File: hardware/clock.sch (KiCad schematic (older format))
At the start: 18 parts, among them P4 CLOCK_PANEL, P5 CLOCK_MAIN, U1 LM555N, U5 TL071, U6 LM2903

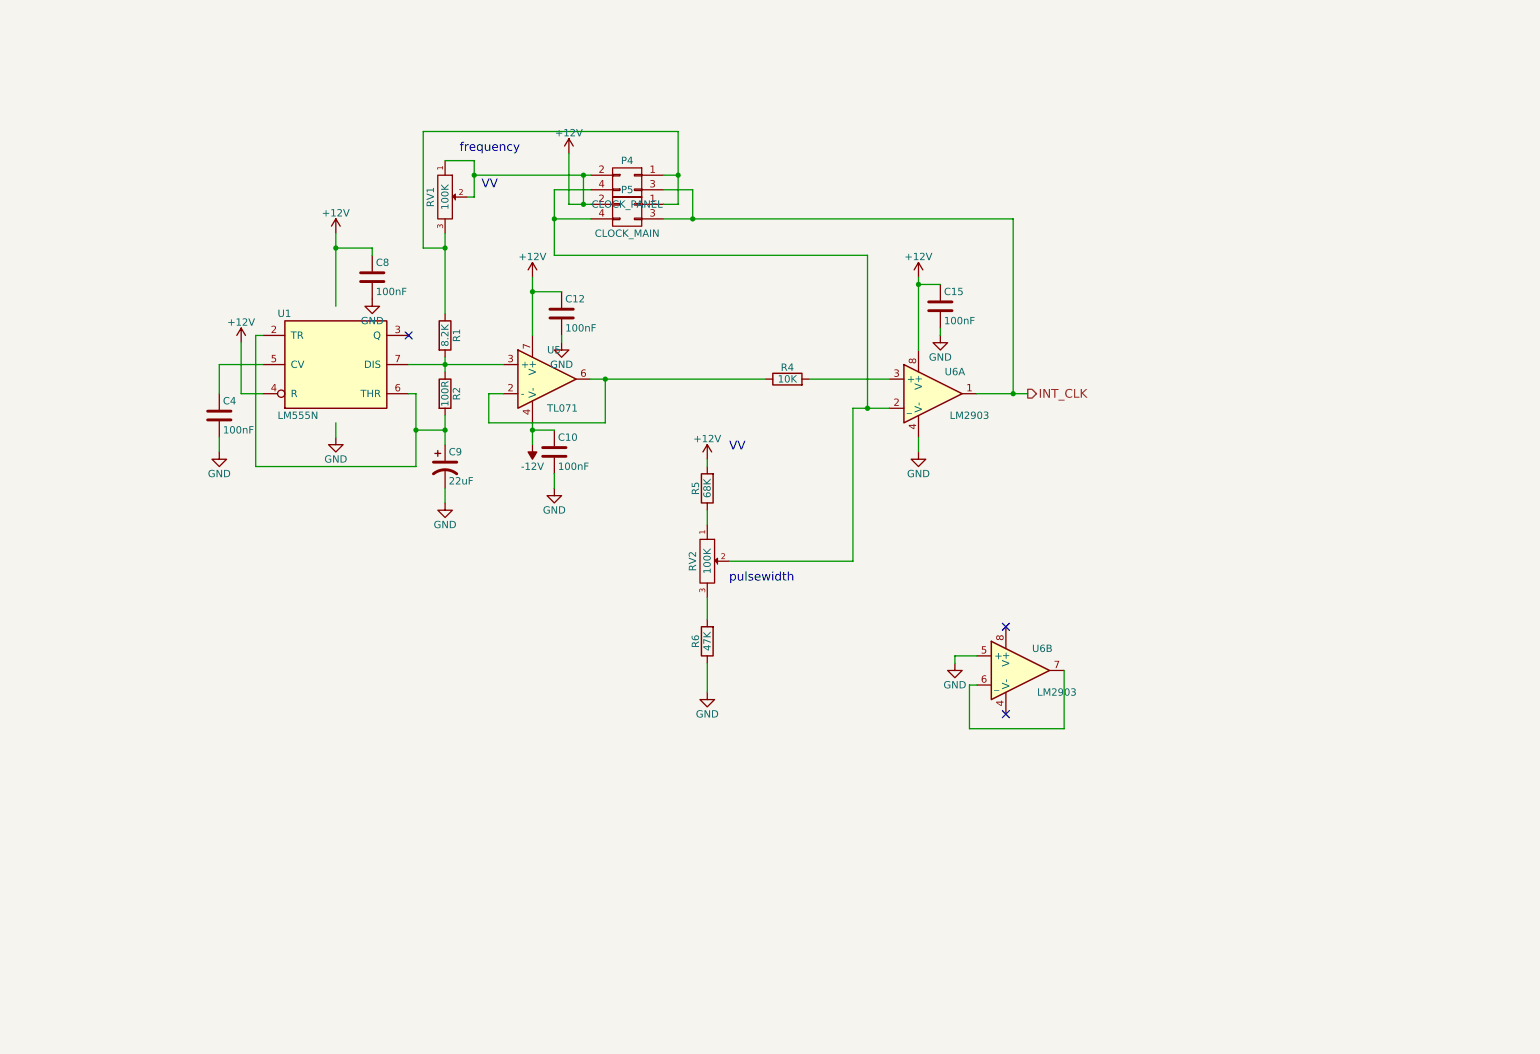
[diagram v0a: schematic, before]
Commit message: replaced old hardware files with the most recent ones tracking CLAUDE.md AI files used in revising the project
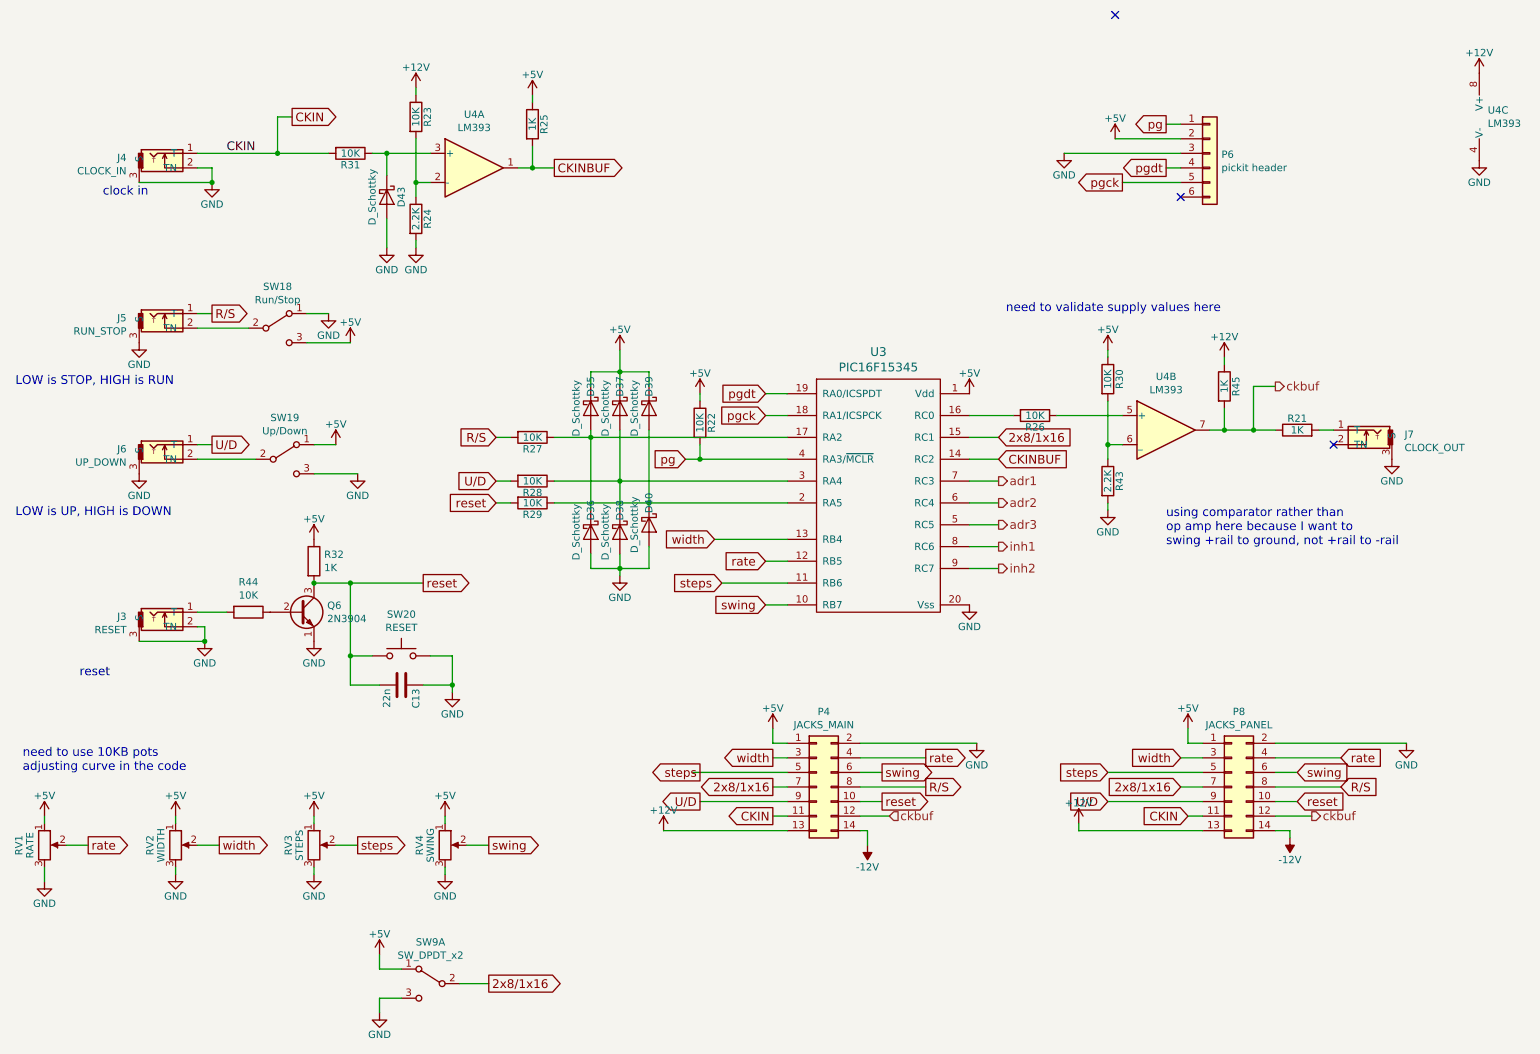
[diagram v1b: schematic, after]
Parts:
- removed C10, C12, C15, C4, C8: 100nF, Capacitors_ThroughHole:C_Rect_L7_W2_P5, symbol C
- removed C9: 22uF, Capacitors_ThroughHole:C_Radial_D5_L11_P2.5, symbol CP1
- removed P4: CLOCK_PANEL, Socket_Strips:Socket_Strip_Straight_2x02, symbol CONN_02X02
- removed P5: CLOCK_MAIN, Pin_Headers:Pin_Header_Straight_2x02, symbol CONN_02X02
- removed R1: 8.2K, Resistors_ThroughHole:Resistor_Horizontal_RM10mm, symbol R
- removed R2: 100R, Resistors_ThroughHole:Resistor_Horizontal_RM10mm, symbol R
- removed R4: 10K, Resistors_ThroughHole:Resistor_Horizontal_RM10mm, symbol R
- removed R5: 68K, Resistors_ThroughHole:Resistor_Horizontal_RM10mm, symbol R
- removed R6: 47K, Resistors_ThroughHole:Resistor_Horizontal_RM10mm, symbol R
- removed RV1, RV2: 100K, Walter Resistors:trimmer_alps-rk09k1130ah1, symbol POT-RESCUE-trigger-seq
- removed U1: LM555N, Housings_DIP:DIP-8_W7.62mm_LongPads, symbol LM555N
- removed U5: TL071, Housings_DIP:DIP-8_W7.62mm_LongPads, symbol TL071
- removed U6: LM2903, symbol LM2903
- added C13: 22n, Capacitor_THT:C_Disc_D7.0mm_W2.5mm_P5.00mm, symbol device:C
- added D35, D36, D37, D38, D39, D40, D43: D_Schottky, Diode_THT:D_DO-35_SOD27_P7.62mm_Horizontal, symbol device:D_Schottky
- added J3: RESET, My Library:thonkiconn, symbol altconnector:AudioJack2_Ground_Switch
- added J4: CLOCK_IN, My Library:thonkiconn, symbol altconnector:AudioJack2_Ground_Switch
- added J5: RUN_STOP, My Library:thonkiconn, symbol altconnector:AudioJack2_Ground_Switch
- added J6: UP_DOWN, My Library:thonkiconn, symbol altconnector:AudioJack2_Ground_Switch
- added J7: CLOCK_OUT, My Library:thonkiconn, symbol altconnector:AudioJack2_Ground_Switch
- added P4: JACKS_MAIN, Connector_PinHeader_2.54mm:PinHeader_2x07_P2.54mm_Vertical, symbol trigger-seq-rescue:Conn_02x07_Odd_Even-Connector
- added P6: pickit header, Connector_PinHeader_2.54mm:PinHeader_1x06_P2.54mm_Vertical, symbol trigger-seq-rescue:Conn_01x06-Connector
- added P8: JACKS_PANEL, Connector_PinSocket_2.54mm:PinSocket_2x07_P2.54mm_Vertical, symbol trigger-seq-rescue:Conn_02x07_Odd_Even-Connector
- added Q6: 2N3904, Package_TO_SOT_THT:TO-92_Inline_Wide, symbol trigger-seq-rescue:2N3904-Transistor
- added R21, R25, R32, R45: 1K, Resistor_THT:R_Axial_DIN0207_L6.3mm_D2.5mm_P10.16mm_Horizontal, symbol device:R
- added R22, R23, R26, R27, R28, R29, R30, R31, R44: 10K, Resistor_THT:R_Axial_DIN0207_L6.3mm_D2.5mm_P10.16mm_Horizontal, symbol device:R
- added R24, R43: 2.2K, Resistor_THT:R_Axial_DIN0207_L6.3mm_D2.5mm_P10.16mm_Horizontal, symbol device:R
- added RV1: RATE, Walter Resistors:trimmer_alps-rk09k1130ah1, symbol trigger-seq-rescue:POT-device
- added RV2: WIDTH, Walter Resistors:trimmer_alps-rk09k1130ah1, symbol trigger-seq-rescue:POT-device
- added RV3: STEPS, Walter Resistors:trimmer_alps-rk09k1130ah1, symbol trigger-seq-rescue:POT-device
- added RV4: SWING, Walter Resistors:trimmer_alps-rk09k1130ah1, symbol trigger-seq-rescue:POT-device
- added SW18: Run/Stop, My Library:submini_toggle_SPDT_2267079, symbol Switch:SW_SPDT
- added SW19: Up/Down, My Library:submini_toggle_SPDT_2267079, symbol Switch:SW_SPDT
- added SW20: RESET, My Library:C&K_round_pushbutton, symbol Switch:SW_Push
- added SW9: SW_DPDT_x2, My Library:submini_toggle_DPDT_wider, symbol Switch:SW_DPDT_x2
- added U3: PIC16F15345, Package_DIP:DIP-20_W7.62mm_LongPads, symbol petelib:PIC16F15345
- added U4: LM393, Package_DIP:DIP-8_W7.62mm_LongPads, symbol Comparators:LM393
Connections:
- net +12V: now also P4.13 (Pin_13), P8.13 (Pin_13), R23.1, R45.1, U4.8 (V+)
- net -12V: now also P4.14 (Pin_14), P8.14 (Pin_14)
- net GND: now also C13.1, D36.2 (A), D38.2 (A), D40.2 (A), D43.2 (A), J3.2 (TN), J3.3 (S), J4.2 (TN), J4.3 (S), J5.3 (S), J6.3 (S), J7.3 (S), P4.2 (Pin_2), P6.3 (Pin_3), P8.2 (Pin_2), Q6.1 (E), R24.2, R43.2, RV1.3, RV2.3, RV3.3, RV4.3, SW18.1 (A), SW19.3 (C), SW20.2, SW9.3 (C), U3.20 (Vss), U4.4 (V-)
- new net: J7.1 (T), R21.2
- new net: R23.2, R24.1, U4.2 (-)
- new net: D35.2 (A), D36.1 (K), R27.1, U3.17 (RA2)
- new net: D37.2 (A), D38.1 (K), R28.1, U3.3 (RA4)
- new net: D39.2 (A), D40.1 (K), R29.1, U3.2 (RA5)
- new net: D43.1 (K), R31.1, U4.3 (+)
- new net: J5.2 (TN), SW18.2 (B)
- new net: J6.2 (TN), SW19.2 (B)
- new net: R26.2, U3.16 (RC0)
- new net: R30.2, R43.1, U4.6 (_)
- new net: R26.1, U4.5 (+)
- new net: Q6.2 (B), R44.1
- new net: J3.1 (T), R44.2
- new net +5V: D35.1 (K), D37.1 (K), D39.1 (K), P4.1 (Pin_1), P6.2 (Pin_2), P8.1 (Pin_1), R22.1, R25.1, R30.1, R32.1, RV1.1, RV2.1, RV3.1, RV4.1, SW18.3 (C), SW19.1 (A), SW9.1 (A), U3.1 (Vdd)
- new net 2x8/1x16: P4.7 (Pin_7), P8.7 (Pin_7), SW9.2 (B), U3.15 (RC1)
- new net CKIN: J4.1 (T), P4.11 (Pin_11), P8.11 (Pin_11), R31.2
- new net CKINBUF: R25.2, U3.14 (RC2), U4.1
- new net R/S: J5.1 (T), P4.8 (Pin_8), P8.8 (Pin_8), R27.2
- new net U/D: J6.1 (T), P4.9 (Pin_9), P8.9 (Pin_9), R28.2
- new net adr1: U3.7 (RC3)
- new net adr2: U3.6 (RC4)
- new net adr3: U3.5 (RC5)
- new net ckbuf: P4.12 (Pin_12), P8.12 (Pin_12), R21.1, R45.2, U4.7
- new net inh1: U3.8 (RC6)
- new net inh2: U3.9 (RC7)
- new net pg: P6.1 (Pin_1), R22.2, U3.4 (RA3/~MCLR)
- new net pgck: P6.5 (Pin_5), U3.18 (RA1/ICSPCK)
- new net pgdt: P6.4 (Pin_4), U3.19 (RA0/ICSPDT)
- new net rate: P4.4 (Pin_4), P8.4 (Pin_4), RV1.2, U3.12 (RB5)
- new net reset: C13.2, P4.10 (Pin_10), P8.10 (Pin_10), Q6.3 (C), R29.2, R32.2, SW20.1
- new net steps: P4.5 (Pin_5), P8.5 (Pin_5), RV3.2, U3.11 (RB6)
- new net swing: P4.6 (Pin_6), P8.6 (Pin_6), RV4.2, U3.10 (RB7)
- new net width: P4.3 (Pin_3), P8.3 (Pin_3), RV2.2, U3.13 (RB4)
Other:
- note added: "LOW is STOP, HIGH is RUN\n"
- note added: "LOW is UP, HIGH is DOWN"
- note added: "clock in"
- note added: "need to use 10KB pots\nadjusting curve in the code"
- note added: "need to validate supply values here"
- note added: "reset"
- note added: "using comparator rather than \nop amp here because I want to\nswing +rail to ground, not +rail to -rail"
- note removed: "VV"
- note removed: "frequency"
- note removed: "pulsewidth"
